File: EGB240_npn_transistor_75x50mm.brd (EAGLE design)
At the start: 49.6 x 44.9 mm, 12 parts, among them Q1 2N4126, U1 74HC14

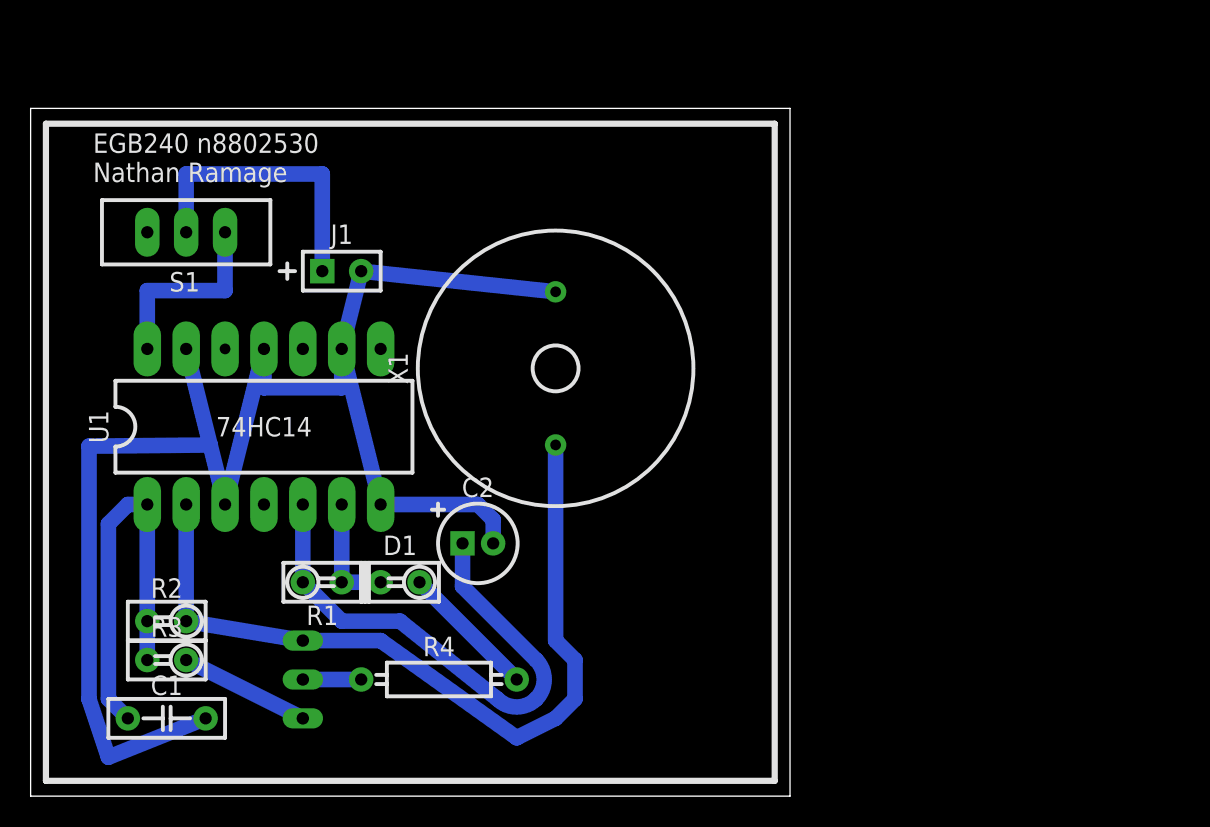
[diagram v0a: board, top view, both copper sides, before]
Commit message: added npn board
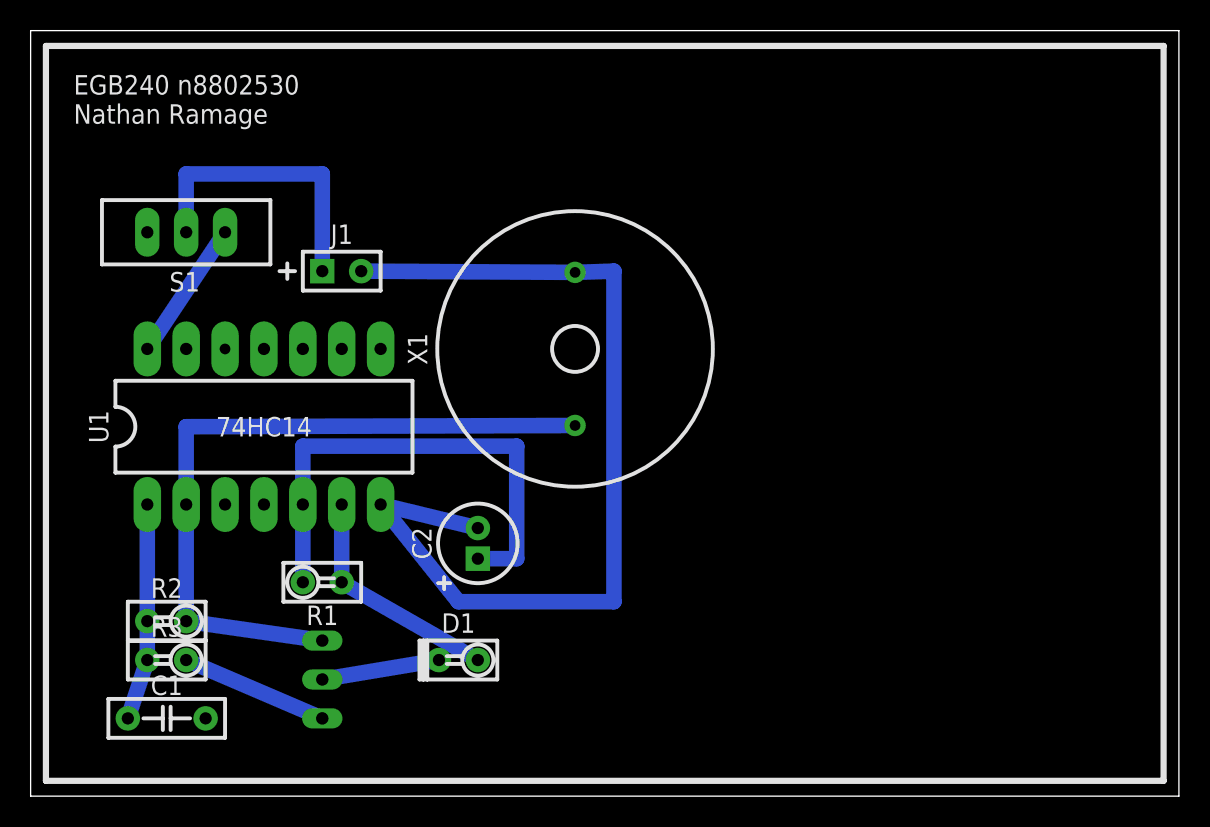
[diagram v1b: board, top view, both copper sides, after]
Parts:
- removed R4: 15k, EGB240:AXIAL-P10.16
- C1: value 15n -> (none)
- C2: value 33u -> (none)
- Q1: value 2N4126 -> BC489; device transistor-pnp:TO92-CBE -> transistor-npn:TO92-EBC
- R1: value 22k -> (none)
- R2: value 15k -> (none)
- R3: value 27k -> (none)
- moved D1 6.35 mm to (27.9, 8.89)
- moved X1 1.80 mm to (35.6, 29.2)
- turned C2 to 90 degrees
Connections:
- removed net N$3: D1.A, R4.P$2
- net GND: no longer U1.P$11, U1.P$13, U1.P$3, U1.P$9
- net N$2: now also D1.A; no longer D1.K
- net N$4: now also D1.K; no longer R4.P$1
- net N$5: now also Q1.E; no longer Q1.C
- net N$7: now also Q1.C; no longer Q1.E
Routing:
- net GND: track 104.2 -> 62.9 mm
- net N$6: track 26.5 -> 14.2 mm
- net N$3: track 8.98 -> 0.00 mm
- net N$2: track 7.62 -> 15.3 mm
- net N$7: track 53.1 -> 47.1 mm
- net N$4: track 3.81 -> 7.73 mm
- net +3V: track 12.7 -> 9.16 mm
- net N$1: track 35.3 -> 32.8 mm
- net N$5: track 8.52 -> 9.67 mm
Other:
- board size 49.6 x 44.9 mm -> 75 x 50 mm

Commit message: Added Gerber files
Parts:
- Q1: value BC489 -> PN100
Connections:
- new net N$3: U1.P$4, X1.P$1
- net GND: now also U1.P$11, U1.P$13, U1.P$9
- net N$7: now also U1.P$3; no longer X1.P$1
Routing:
- net GND: track 62.9 -> 117.7 mm
- net N$7: track 47.1 -> 19.1 mm
- net N$3: track 0.00 -> 25.5 mm
- net +3V: track 9.16 -> 9.96 mm
- net N$2: track 15.3 -> 16.0 mm
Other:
- board size 75 x 50 mm -> 44.5 x 43.6 mm
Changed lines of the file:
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@@
 <board>
 <plain>
-<wire x1="0" y1="0" x2="75" y2="0" width="0" layer="20"/>
-<wire x1="75" y1="0" x2="75" y2="50" width="0" layer="20"/>
-<wire x1="75" y1="50" x2="0" y2="50" width="0" layer="20"/>
-<wire x1="0" y1="50" x2="0" y2="0" width="0" layer="20"/>
-<text x="2.81" y="43.92" size="1.27" layer="21" font="vector" ratio="12" rot="SR0">EGB240 n8802530
+<wire x1="2.54" y1="0" x2="47.06" y2="0" width="0" layer="20"/>
+<wire x1="47.06" y1="0" x2="47.06" y2="43.65" width="0" layer="20"/>
+<wire x1="47.06" y1="43.65" x2="2.54" y2="43.65" width="0" layer="20"/>
+<wire x1="2.54" y1="43.65" x2="2.54" y2="0" width="0" layer="20"/>
+<text x="26.94" y="3.28" size="1.27" layer="21" font="vector" ratio="12" rot="SR0">EGB240 n8802530
 Nathan Ramage</text>
-<wire x1="1" y1="1" x2="1" y2="49" width="0.4064" layer="21"/>
-<wire x1="1" y1="49" x2="74" y2="49" width="0.4064" layer="21"/>
-<wire x1="74" y1="49" x2="74" y2="1" width="0.4064" layer="21"/>
-<wire x1="74" y1="1" x2="1" y2="1" width="0.4064" layer="21"/>
-<wire x1="0" y1="50" x2="0" y2="0" width="2" layer="40"/>
-<wire x1="0" y1="0" x2="75" y2="0" width="2" layer="40"/>
-<wire x1="75" y1="0" x2="75" y2="50" width="2" layer="40"/>
-<wire x1="75" y1="50" x2="0" y2="50" width="2" layer="40"/>
+<wire x1="3.54" y1="1" x2="3.54" y2="42.65" width="0.4064" layer="21"/>
+<wire x1="3.54" y1="42.65" x2="46.06" y2="42.65" width="0.4064" layer="21"/>
+<wire x1="46.06" y1="42.65" x2="46.06" y2="1" width="0.4064" layer="21"/>
+<wire x1="46.06" y1="1" x2="3.54" y2="1" width="0.4064" layer="21"/>
+<wire x1="2.54" y1="43.65" x2="2.54" y2="0" width="2" layer="40"/>
+<wire x1="2.54" y1="0" x2="47.06" y2="0" width="2" layer="40"/>
+<wire x1="47.06" y1="0" x2="47.06" y2="43.65" width="2" layer="40"/>
+<wire x1="47.06" y1="43.65" x2="2.54" y2="43.65" width="2" layer="40"/>
 </plain>
 <attributes>
@@
 <element name="U1" library="EGB240" package="DIP-14" value="74HC14" x="15.24" y="24.13" rot="R90"/>
 <element name="R1" library="EGB240" package="AXIAL-P2.54" value="" x="19.05" y="13.97" rot="R180"/>
-<element name="R2" library="EGB240" package="AXIAL-P2.54" value="" x="8.89" y="11.43"/>
-<element name="C1" library="EGB240" package="CAP-DISC-P5.08" value="" x="8.89" y="5.08"/>
+<element name="R2" library="EGB240" package="AXIAL-P2.54" value="" x="8.89" y="11.43" smashed="yes">
+<attribute name="NAME" x="8.89" y="12.954" size="1.27" layer="21" align="bottom-center"/>
+</element>
+<element name="C1" library="EGB240" package="CAP-DISC-P5.08" value="" x="8.89" y="5.08" smashed="yes">
+<attribute name="NAME" x="8.89" y="1.524" size="1.27" layer="21" align="bottom-center"/>
+</element>
 <element name="J1" library="EGB240" package="BATT-3V" value="" x="20.32" y="34.29"/>
 <element name="S1" library="EGB240" package="SS-12" value="" x="10.16" y="36.83" rot="R90"/>
 <element name="X1" library="EGB240" package="PS1720P02" value="" x="35.56" y="29.21" rot="R90"/>
 <element name="C2" library="EGB240" package="CAP-RB-P2.0-D5.0" value="" x="29.21" y="16.51" rot="R90"/>
-<element name="R3" library="EGB240" package="AXIAL-P2.54" value="" x="8.89" y="8.89"/>
+<element name="R3" library="EGB240" package="AXIAL-P2.54" value="" x="8.89" y="8.89" smashed="yes">
+<attribute name="NAME" x="5.08" y="7.874" size="1.27" layer="21" align="bottom-center"/>
+</element>
 <element name="D1" library="EGB240" package="DO35-P2.54" value="" x="27.94" y="8.89"/>
-<element name="Q1" library="transistor-npn" package="TO92-EBC" value="BC489" x="17.78" y="7.62" rot="MR270"/>
+<element name="Q1" library="transistor-npn" package="TO92-EBC" value="PN100" x="17.78" y="7.62" smashed="yes" rot="MR270">
+<attribute name="NAME" x="14.732" y="10.16" size="1.27" layer="25" ratio="10" rot="R270"/>
+<attribute name="VALUE" x="21.082" y="10.16" size="1.27" layer="27" ratio="10" rot="R270"/>
+</element>
 </elements>
 <signals>
@@
 <contactref element="C2" pad="P$2"/>
 <contactref element="C1" pad="P$2"/>
-<contactref element="X1" pad="P$2"/>
 <contactref element="J1" pad="P$2"/>
 <wire x1="29.21" y1="17.51" x2="22.86" y2="19.05" width="1.016" layer="16"/>
 <wire x1="22.86" y1="19.05" x2="27.94" y2="12.7" width="1.016" layer="16"/>
-<wire x1="27.94" y1="12.7" x2="38.1" y2="12.7" width="1.016" layer="16"/>
-<wire x1="38.1" y1="12.7" x2="38.1" y2="34.29" width="1.016" layer="16"/>
-<wire x1="38.1" y1="34.29" x2="35.56" y2="34.21" width="1.016" layer="16"/>
-<wire x1="11.43" y1="5.08" x2="22.86" y2="19.05" width="0" layer="19" extent="1-1"/>
-<wire x1="35.56" y1="34.21" x2="21.59" y2="34.29" width="1.016" layer="16"/>
+<wire x1="27.94" y1="12.7" x2="34.29" y2="12.7" width="1.016" layer="16"/>
+<wire x1="34.29" y1="12.7" x2="38.1" y2="12.7" width="1.016" layer="16"/>
+<wire x1="38.1" y1="12.7" x2="38.1" y2="34.21" width="1.016" layer="16"/>
+<wire x1="11.43" y1="5.08" x2="19.05" y2="2.54" width="1.016" layer="16"/>
+<wire x1="19.05" y1="2.54" x2="34.29" y2="7.62" width="1.016" layer="16"/>
+<wire x1="34.29" y1="7.62" x2="34.29" y2="12.7" width="1.016" layer="16"/>
+<contactref element="X1" pad="P$2"/>
+<wire x1="21.59" y1="34.29" x2="35.56" y2="34.29" width="1.016" layer="16"/>
+<wire x1="35.56" y1="34.29" x2="35.56" y2="34.21" width="1.016" layer="16"/>
+<wire x1="35.56" y1="34.21" x2="38.1" y2="34.21" width="1.016" layer="16"/>
+<wire x1="38.1" y1="34.21" x2="38.1" y2="34.29" width="1.016" layer="16"/>
+<contactref element="U1" pad="P$9"/>
+<contactref element="U1" pad="P$11"/>
+<contactref element="U1" pad="P$13"/>
+<wire x1="20.32" y1="29.21" x2="20.917646875" y2="31.6005875" width="1.016" layer="16"/>
+<wire x1="20.917646875" y1="31.6005875" x2="21.59" y2="34.29" width="1.016" layer="16"/>
+<wire x1="10.16" y1="29.21" x2="10.16" y2="25.4" width="1.016" layer="16"/>
+<wire x1="10.16" y1="25.4" x2="15.24" y2="26.67" width="1.016" layer="16"/>
+<wire x1="15.24" y1="26.67" x2="15.24" y2="29.21" width="1.016" layer="16"/>
+<wire x1="15.24" y1="29.21" x2="16.51" y2="33.02" width="1.016" layer="16"/>
+<wire x1="16.51" y1="33.02" x2="20.917646875" y2="31.6005875" width="1.016" layer="16"/>
 </signal>
 <signal name="N$1">
@@
 <contactref element="D1" pad="A"/>
 <wire x1="20.32" y1="19.05" x2="20.32" y2="13.97" width="1.016" layer="16"/>
-<wire x1="29.21" y1="8.89" x2="20.32" y2="13.97" width="1.016" layer="16"/>
+<wire x1="20.32" y1="13.97" x2="25.4" y2="11.43" width="1.016" layer="16"/>
+<wire x1="25.4" y1="11.43" x2="29.21" y2="10.16" width="1.016" layer="16"/>
+<wire x1="29.21" y1="10.16" x2="29.21" y2="8.89" width="1.016" layer="16"/>
 </signal>
 <signal name="N$4">
@@
 <signal name="N$7">
 <contactref element="R2" pad="P$2"/>
-<contactref element="X1" pad="P$1"/>
-<contactref element="U1" pad="P$2"/>
 <contactref element="Q1" pad="C"/>
 <wire x1="19.05" y1="10.16" x2="10.16" y2="11.43" width="1.016" layer="16"/>
+<contactref element="U1" pad="P$2"/>
+<contactref element="U1" pad="P$3"/>
 <wire x1="10.16" y1="11.43" x2="10.16" y2="19.05" width="1.016" layer="16"/>
-<wire x1="35.56" y1="24.21" x2="10.16" y2="24.13" width="1.016" layer="16"/>
-<wire x1="10.16" y1="24.13" x2="10.16" y2="19.05" width="1.016" layer="16"/>
+<wire x1="10.16" y1="19.05" x2="12.7" y2="19.05" width="1.016" layer="16"/>
 </signal>
 <signal name="N$8">
@@
 <contactref element="S1" pad="3"/>
 <contactref element="U1" pad="P$14"/>
-<wire x1="12.7" y1="36.83" x2="7.62" y2="29.21" width="1.016" layer="16"/>
+<wire x1="12.7" y1="36.83" x2="11.43" y2="34.29" width="1.016" layer="16"/>
+<wire x1="11.43" y1="34.29" x2="7.62" y2="31.75" width="1.016" layer="16"/>
+<wire x1="7.62" y1="31.75" x2="7.62" y2="29.21" width="1.016" layer="16"/>
+</signal>
+<signal name="N$3">
+<contactref element="X1" pad="P$1"/>
+<contactref element="U1" pad="P$4"/>
+<wire x1="35.56" y1="24.21" x2="15.24" y2="24.21" width="1.016" layer="16"/>
+<wire x1="15.24" y1="24.21" x2="15.24" y2="19.05" width="1.016" layer="16"/>
 </signal>
 </signals>
